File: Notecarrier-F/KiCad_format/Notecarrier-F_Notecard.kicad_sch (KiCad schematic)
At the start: 20 parts, among them J5 NanoSIM - SF72S006VBAR2500, J6 MDT420E01001, SW1 CJS-1200TA, SW2 PTS810SJK250SMTRLFS

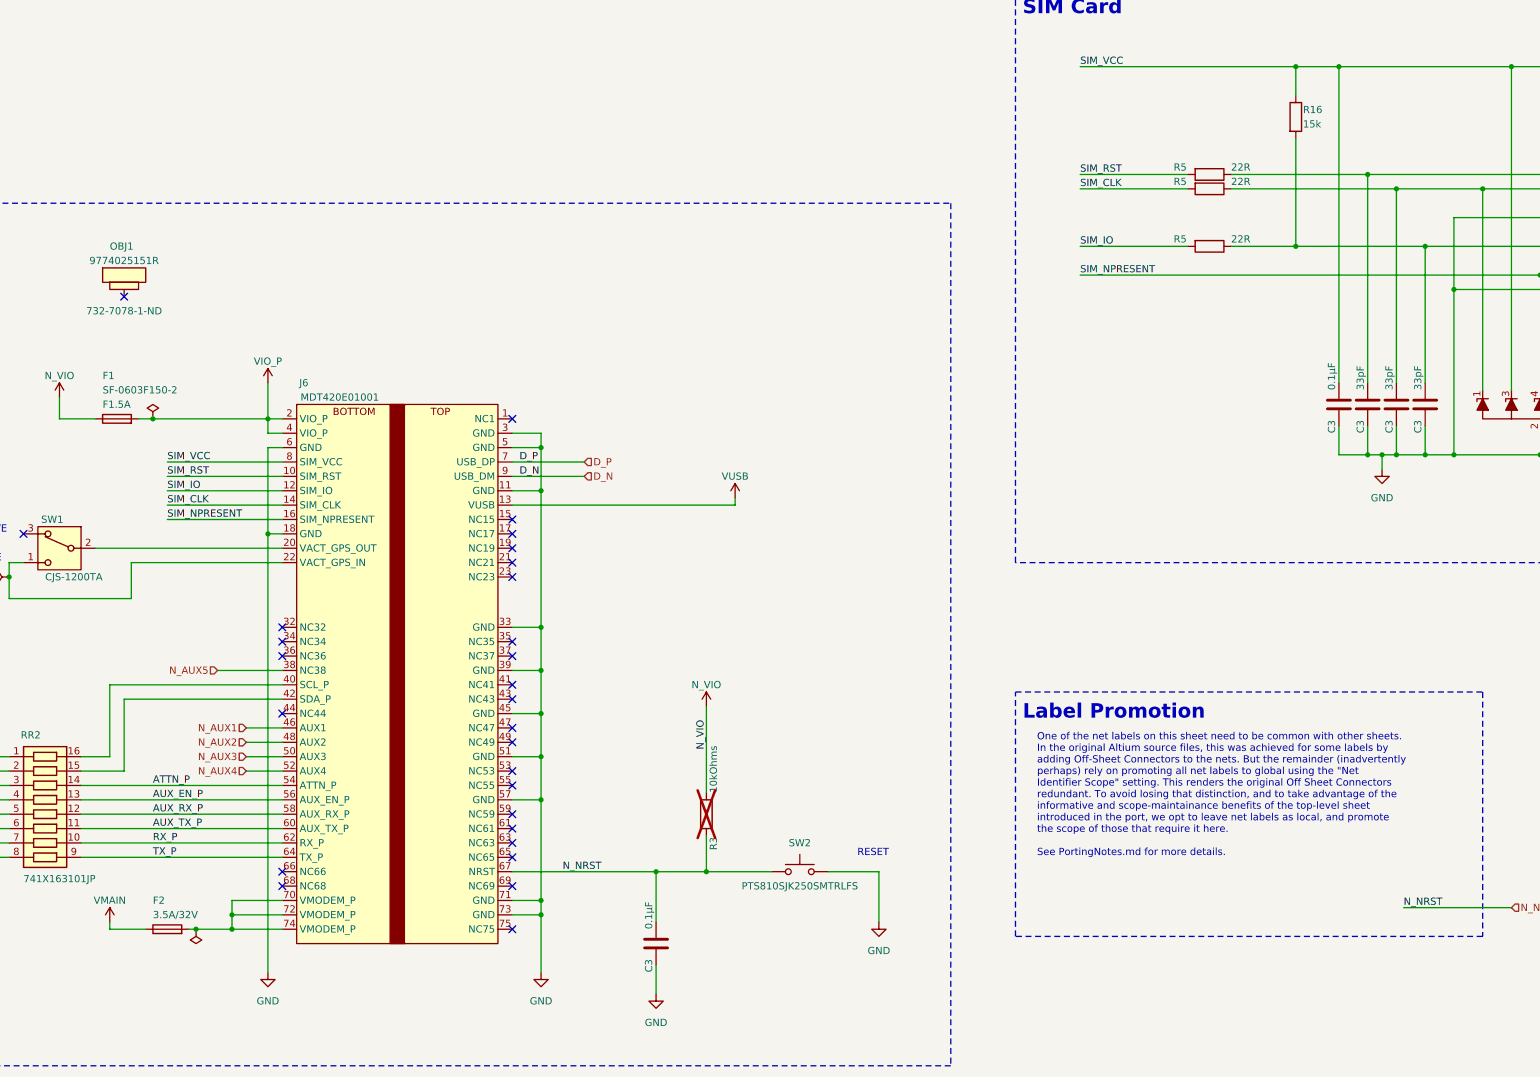
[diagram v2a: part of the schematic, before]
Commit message: Finish first pass PCB port.
Still need to go back and finalise top-level schematic sheet.
Next step is validation where there’s bound to be lots of copper rules to tweak.
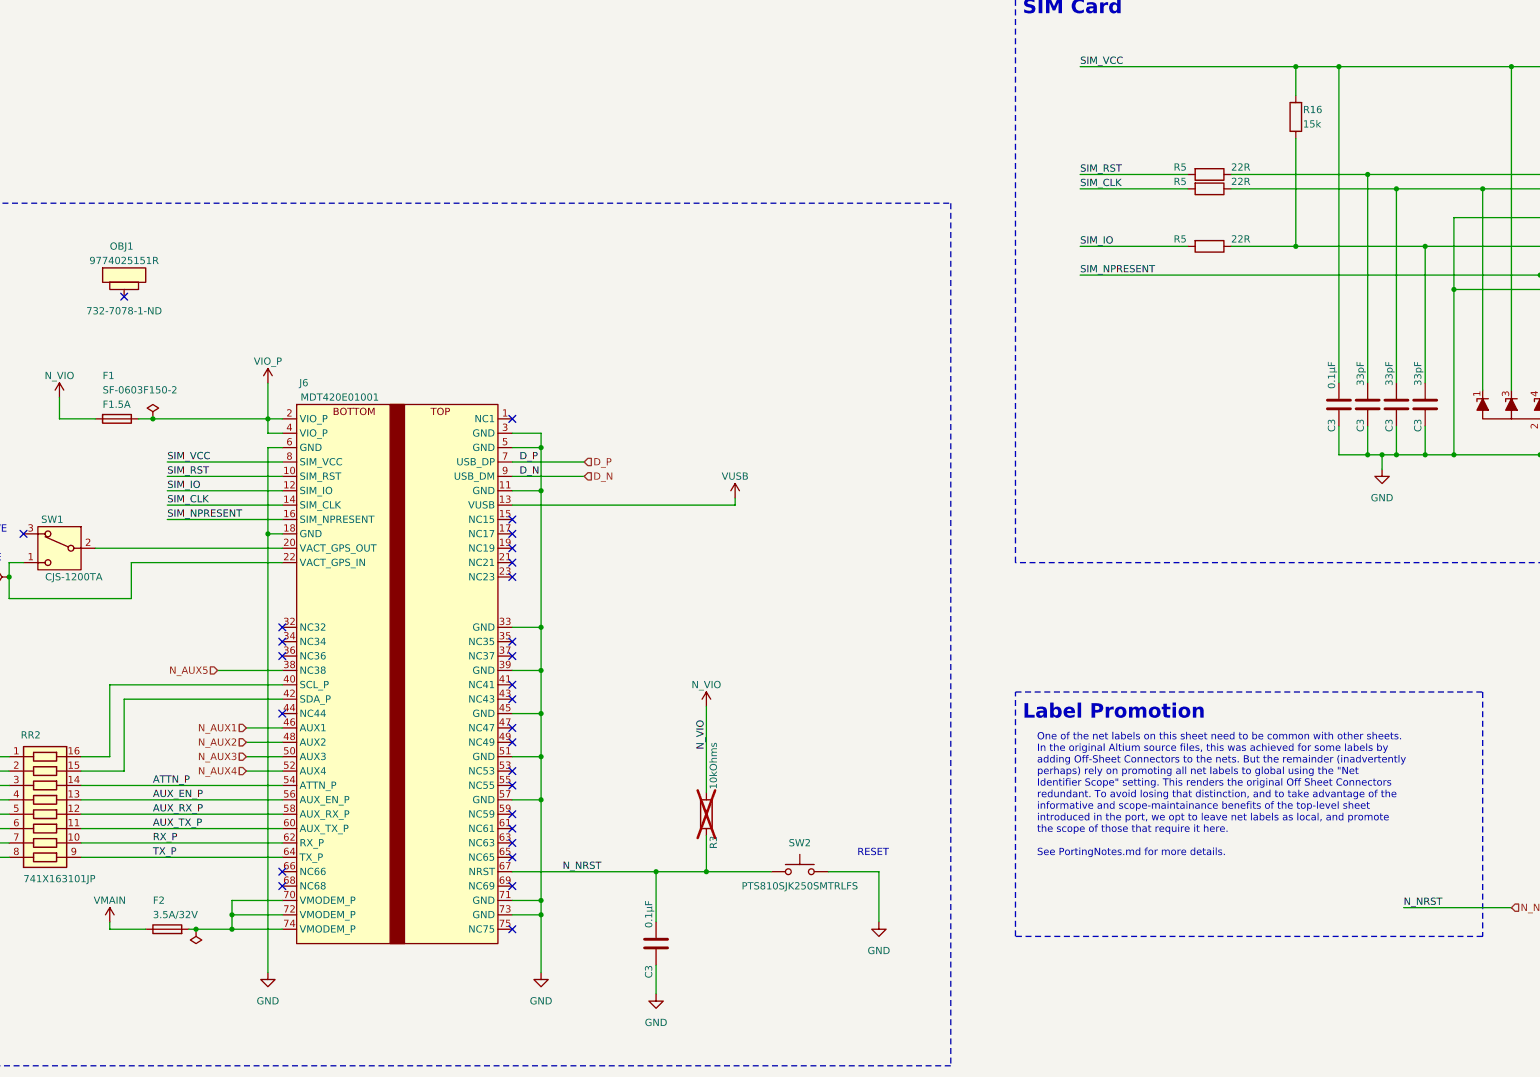
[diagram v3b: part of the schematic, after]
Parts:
- OBJ1: footprint blues-kicad-lib:DIST-WASMSIM0250 -> blues-kicad-lib:9774025151R
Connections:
- net GND: now also C3.1, C3.1, C3.1, C3.1, C3.1; no longer C3.2, C3.2, C3.2, C3.2, C3.2
- net N_NRST: now also C3.2, R3.1; no longer C3.1, R3.2
- net N_VIO: now also F1.2, R3.2; no longer F1.1, R3.1
- net SIM_VCC: now also C3.2, R16.2; no longer C3.1, R16.1
- net VIO_P: now also F1.1; no longer F1.2
- net at J5.C3 (CLK), R5.1, TVS2.1 (K1): now also C3.2; no longer C3.1
- net at J5.C7 (I/O), R5.1, TVS2.6 (K5): now also C3.2, R16.1; no longer C3.1, R16.2
- net at J5.C2 (RST), R5.1, TVS2.5 (K4): now also C3.2; no longer C3.1
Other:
- moved on the sheet: C3, F1, R16, R3
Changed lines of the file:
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@@
     )
   )
-  (symbol (lib_id "Device:C") (at 300.99 110.49 0) (unit 1)
-    (in_bom yes) (on_board yes) (dnp no)
-    (property "Reference" "C3" (at 299.72 115.57 90)
-      (effects (font (size 1.27 1.27)) (justify left))
-    )
-    (property "Value" "0.1µF" (at 299.72 107.95 90)
-      (effects (font (size 1.27 1.27)) (justify left))
-    )
-    (property "Footprint" "blues-kicad-lib-pending:CAP 0402_1005" (at 301.9552 114.3 0)
+  (symbol (lib_id "Device:C") (at 300.99 110.49 180) (unit 1)
+    (in_bom yes) (on_board yes) (dnp no)
+    (property "Reference" "C3" (at 299.72 113.03 90)
+      (effects (font (size 1.27 1.27)) (justify left))
+    )
+    (property "Value" "0.1µF" (at 299.72 102.87 90)
+      (effects (font (size 1.27 1.27)) (justify left))
+    )
+    (property "Footprint" "blues-kicad-lib-pending:CAP 0402_1005" (at 300.0248 106.68 0)
       (effects (font (size 1.27 1.27)) hide)
     )
@@
     )
   )
-  (symbol (lib_id "Device:C") (at 311.15 110.49 0) (unit 1)
-    (in_bom yes) (on_board yes) (dnp no)
-    (property "Reference" "C3" (at 309.88 115.57 90)
-      (effects (font (size 1.27 1.27)) (justify left))
-    )
-    (property "Value" "33pF" (at 309.88 107.95 90)
-      (effects (font (size 1.27 1.27)) (justify left))
-    )
-    (property "Footprint" "blues-kicad-lib-pending:CAP 0402_1005" (at 312.1152 114.3 0)
+  (symbol (lib_id "Device:C") (at 311.15 110.49 180) (unit 1)
+    (in_bom yes) (on_board yes) (dnp no)
+    (property "Reference" "C3" (at 309.88 113.03 90)
+      (effects (font (size 1.27 1.27)) (justify left))
+    )
+    (property "Value" "33pF" (at 309.88 102.87 90)
+      (effects (font (size 1.27 1.27)) (justify left))
+    )
+    (property "Footprint" "blues-kicad-lib-pending:CAP 0402_1005" (at 310.1848 106.68 0)
       (effects (font (size 1.27 1.27)) hide)
     )
@@
     )
   )
-  (symbol (lib_id "Device:C") (at 316.23 110.49 0) (unit 1)
-    (in_bom yes) (on_board yes) (dnp no)
-    (property "Reference" "C3" (at 314.96 115.57 90)
-      (effects (font (size 1.27 1.27)) (justify left))
-    )
-    (property "Value" "33pF" (at 314.96 107.95 90)
-      (effects (font (size 1.27 1.27)) (justify left))
-    )
-    (property "Footprint" "blues-kicad-lib-pending:CAP 0402_1005" (at 317.1952 114.3 0)
+  (symbol (lib_id "Device:C") (at 316.23 110.49 180) (unit 1)
+    (in_bom yes) (on_board yes) (dnp no)
+    (property "Reference" "C3" (at 314.96 113.03 90)
+      (effects (font (size 1.27 1.27)) (justify left))
+    )
+    (property "Value" "33pF" (at 314.96 102.87 90)
+      (effects (font (size 1.27 1.27)) (justify left))
+    )
+    (property "Footprint" "blues-kicad-lib-pending:CAP 0402_1005" (at 315.2648 106.68 0)
       (effects (font (size 1.27 1.27)) hide)
     )
@@
     )
   )
-  (symbol (lib_id "Device:C") (at 180.34 205.74 0) (unit 1)
-    (in_bom yes) (on_board yes) (dnp no)
-    (property "Reference" "C3" (at 179.07 210.82 90)
-      (effects (font (size 1.27 1.27)) (justify left))
-    )
-    (property "Value" "0.1µF" (at 179.07 203.2 90)
-      (effects (font (size 1.27 1.27)) (justify left))
-    )
-    (property "Footprint" "blues-kicad-lib-pending:CAP 0402_1005" (at 181.3052 209.55 0)
+  (symbol (lib_id "Device:C") (at 180.34 205.74 180) (unit 1)
+    (in_bom yes) (on_board yes) (dnp no)
+    (property "Reference" "C3" (at 179.07 209.55 90)
+      (effects (font (size 1.27 1.27)) (justify left))
+    )
+    (property "Value" "0.1µF" (at 179.07 198.12 90)
+      (effects (font (size 1.27 1.27)) (justify left))
+    )
+    (property "Footprint" "blues-kicad-lib-pending:CAP 0402_1005" (at 179.3748 201.93 0)
       (effects (font (size 1.27 1.27)) hide)
     )
@@
       (effects (font (size 1.27 1.27)))
     )
-    (property "Footprint" "blues-kicad-lib:DIST-WASMSIM0250" (at 86.36 101.6 0)
+    (property "Footprint" "blues-kicad-lib:9774025151R" (at 86.36 101.6 0)
       (effects (font (size 1.27 1.27)) hide)
     )
@@
     )
   )
-  (symbol (lib_id "Device:C") (at 306.07 110.49 0) (unit 1)
-    (in_bom yes) (on_board yes) (dnp no)
-    (property "Reference" "C3" (at 304.8 115.57 90)
-      (effects (font (size 1.27 1.27)) (justify left))
-    )
-    (property "Value" "33pF" (at 304.8 107.95 90)
-      (effects (font (size 1.27 1.27)) (justify left))
-    )
-    (property "Footprint" "blues-kicad-lib-pending:CAP 0402_1005" (at 307.0352 114.3 0)
+  (symbol (lib_id "Device:C") (at 306.07 110.49 180) (unit 1)
+    (in_bom yes) (on_board yes) (dnp no)
+    (property "Reference" "C3" (at 304.8 113.03 90)
+      (effects (font (size 1.27 1.27)) (justify left))
+    )
+    (property "Value" "33pF" (at 304.8 102.87 90)
+      (effects (font (size 1.27 1.27)) (justify left))
+    )
+    (property "Footprint" "blues-kicad-lib-pending:CAP 0402_1005" (at 305.1048 106.68 0)
       (effects (font (size 1.27 1.27)) hide)
     )
@@
     )
   )
-  (symbol (lib_id "Device:Fuse") (at 85.09 113.03 90) (unit 1)
+  (symbol (lib_id "Device:Fuse") (at 85.09 113.03 270) (unit 1)
     (in_bom yes) (on_board yes) (dnp no)
     (property "Reference" "F1" (at 82.55 105.41 90)
+      (effects (font (size 1.27 1.27)) (justify left))
+    )
+    (property "Value" "F1.5A" (at 82.55 110.49 90)
+      (effects (font (size 1.27 1.27)) (justify left))
+    )
+    (property "Footprint" "blues-kicad-lib:FS-0603" (at 85.09 111.252 90)
+      (effects (font (size 1.27 1.27)) hide)
+    )
+    (property "Datasheet" "~" (at 85.09 113.03 0)
+      (effects (font (size 1.27 1.27)) hide)
+    )
+    (property "Critical" "" (at 85.09 113.03 0)
+      (effects (font (size 1.27 1.27)) hide)
+    )
+    (property "Description" "FUSIBILE RAPIDO 1.5A 32V 0603 SF-0603F150-2 BOURNS SMT" (at 85.09 113.03 0)
+      (effects (font (size 1.27 1.27)) hide)
+    )
+    (property "Manufacturer" "" (at 85.09 113.03 0)
+      (effects (font (size 1.27 1.27)) hide)
+    )
+    (property "Order Code" "" (at 85.09 113.03 0)
+      (effects (font (size 1.27 1.27)) hide)
+    )
+    (property "Part Number" "SF-0603F150-2" (at 82.55 107.95 90)
+      (effects (font (size 1.27 1.27)) (justify left))
+    )
+    (property "Supplier" "FAE" (at 85.09 113.03 0)
+      (effects (font (size 1.27 1.27)) hide)
+    )
+    (pin "1")
+    (pin "2")
+    (instances
+      (project "Notecarrier-F"
+        (path "/3e57c059-f782-40ac-b9a3-c1636ed27a63/e1550e15-b436-4be3-9685-75e1568dff4b"
+          (reference "F1") (unit 1)
+        )
+      )
+    )
+  )
+  (symbol (lib_id "Device:R") (at 293.37 59.69 180) (unit 1)
+    (in_bom yes) (on_board yes) (dnp no)
+    (property "Reference" "R16" (at 294.64 58.42 0)
       (effects (font (size 1.27 1.27)) (justify right))
     )
-    (property "Value" "F1.5A" (at 82.55 110.49 90)
+    (property "Value" "15k" (at 294.64 60.96 0)
       (effects (font (size 1.27 1.27)) (justify right))
     )
-    (property "Footprint" "blues-kicad-lib:FS-0603" (at 85.09 114.808 90)
-      (effects (font (size 1.27 1.27)) hide)
-    )
-    (property "Datasheet" "~" (at 85.09 113.03 0)
-      (effects (font (size 1.27 1.27)) hide)
-    )
-    (property "Critical" "" (at 85.09 113.03 0)
-      (effects (font (size 1.27 1.27)) hide)
-    )
-    (property "Description" "FUSIBILE RAPIDO 1.5A 32V 0603 SF-0603F150-2 BOURNS SMT" (at 85.09 113.03 0)
-      (effects (font (size 1.27 1.27)) hide)
-    )
-    (property "Manufacturer" "" (at 85.09 113.03 0)
-      (effects (font (size 1.27 1.27)) hide)
-    )
-    (property "Order Code" "" (at 85.09 113.03 0)
-      (effects (font (size 1.27 1.27)) hide)
-    )
-    (property "Part Number" "SF-0603F150-2" (at 82.55 107.95 90)
-      (effects (font (size 1.27 1.27)) (justify right))
-    )
-    (property "Supplier" "FAE" (at 85.09 113.03 0)
-      (effects (font (size 1.27 1.27)) hide)
-    )
-    (pin "1")
-    (pin "2")
-    (instances
-      (project "Notecarrier-F"
-        (path "/3e57c059-f782-40ac-b9a3-c1636ed27a63/e1550e15-b436-4be3-9685-75e1568dff4b"
-          (reference "F1") (unit 1)
-        )
-      )
-    )
-  )
-  (symbol (lib_id "Device:R") (at 293.37 59.69 0) (unit 1)
-    (in_bom yes) (on_board yes) (dnp no)
-    (property "Reference" "R16" (at 294.64 58.42 0)
-      (effects (font (size 1.27 1.27)) (justify left))
-    )
-    (property "Value" "15k" (at 294.64 60.96 0)
-      (effects (font (size 1.27 1.27)) (justify left))
-    )
-    (property "Footprint" "blues-kicad-lib-pending:RES 0402_1005" (at 291.592 59.69 90)
+    (property "Footprint" "blues-kicad-lib-pending:RES 0402_1005" (at 295.148 59.69 90)
       (effects (font (size 1.27 1.27)) hide)
     )
@@
     )
   )
-  (symbol (lib_id "Device:R") (at 189.23 182.88 0) (unit 1)
+  (symbol (lib_id "Device:R") (at 189.23 182.88 180) (unit 1)
     (in_bom yes) (on_board yes) (dnp yes)
-    (property "Reference" "R3" (at 190.5 189.23 90)
-      (effects (font (size 1.27 1.27)) (justify left))
-    )
-    (property "Value" "10kOhms" (at 190.5 179.07 90)
-      (effects (font (size 1.27 1.27)) (justify left))
-    )
-    (property "Footprint" "blues-kicad-lib-pending:RES 0402_1005" (at 187.452 182.88 90)
-      (effects (font (size 1.27 1.27)) hide)
-    )
+    (property "Reference" "R3" (at 190.5 186.69 90)
+      (effects (font (size 1.27 1.27)) (justify left))
+    )
+    (property "Value" "10kOhms" (at 190.5 170.18 90)
+      (effects (font (size 1.27 1.27)) (justify left))
+    )
+    (property "Footprint" "blues-kicad-lib-pending:RES 0402_1005" (at 191.008 182.88 90)
+      (effects (font (size 1.27 1.27)) hide)
+    )
